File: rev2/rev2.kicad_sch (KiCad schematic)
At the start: 106 parts, among them J1 USB_C_Receptacle_USB2.0_14P, SW1 SW_SPDT, SW2 SW_SPDT, SW3 SW_SPDT, SW4 SW_SPDT, SW5 SW_SPDT, SW6 SW_SPDT, SW7 SW_SPDT, SW8 SW_SPDT, U1 ATtiny1604-SS, U2 CH340N, U3 74HC595, U4 74HC595, U5 74HC595, U6 74HC595, U7 74HC595, U8 74HC595

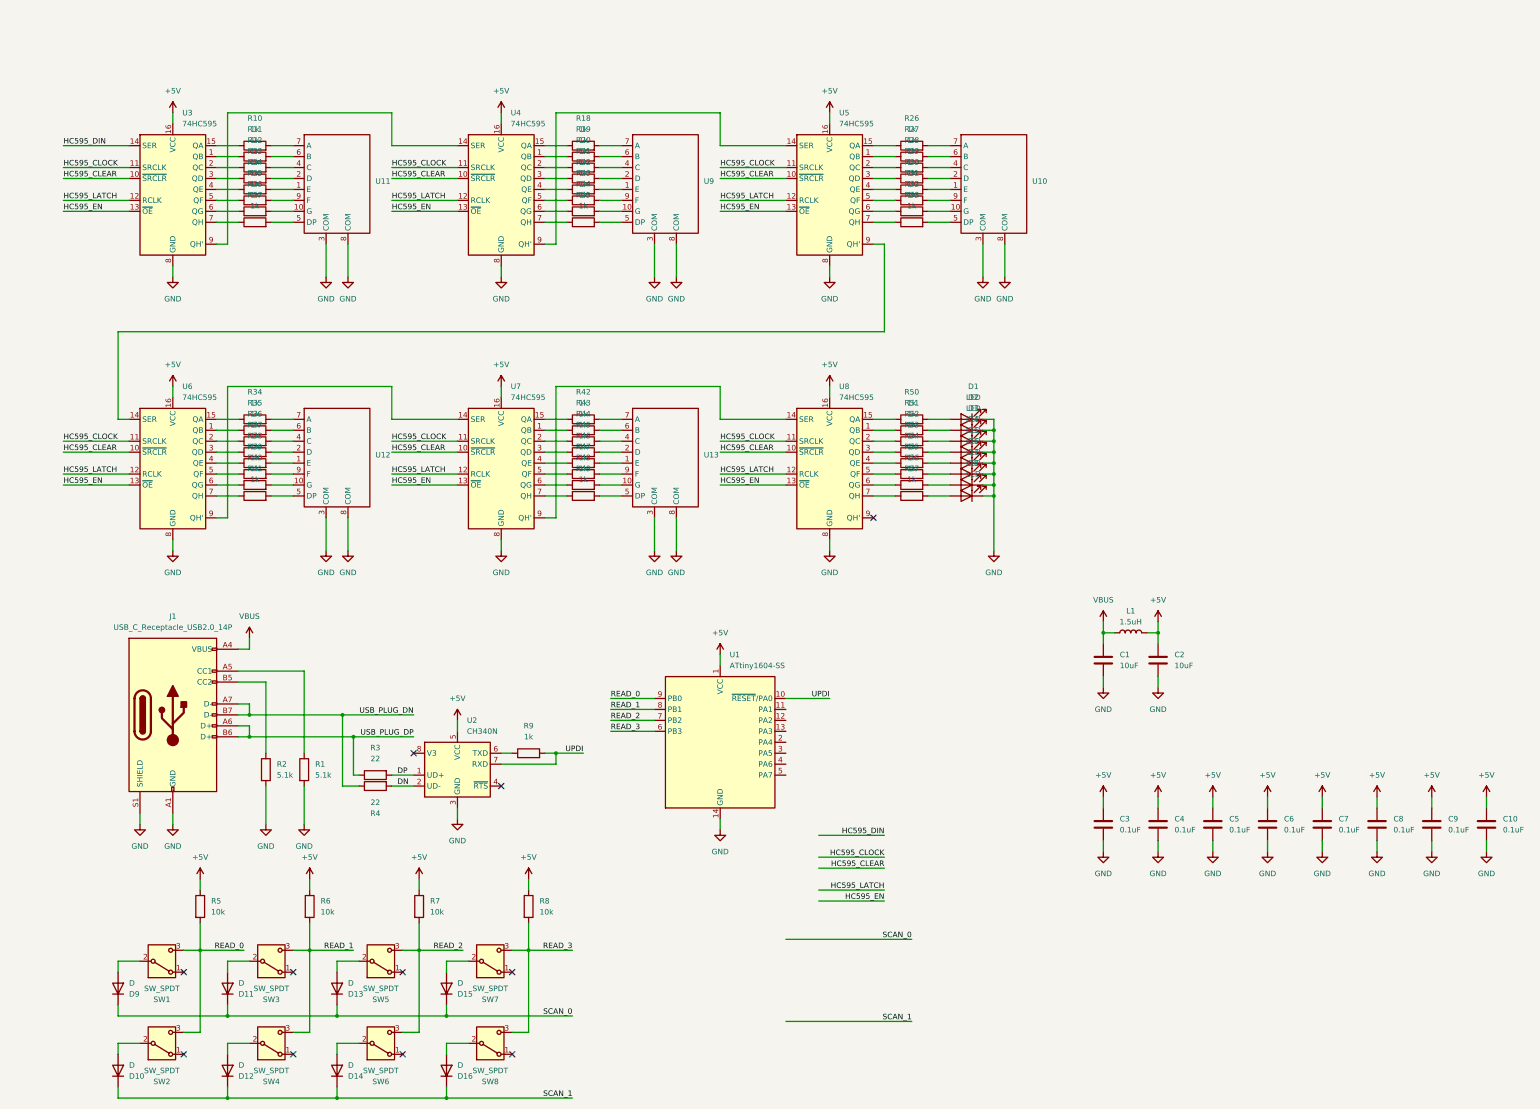
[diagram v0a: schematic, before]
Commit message: ドットマトリックスを追加してダイナミック点灯に変更
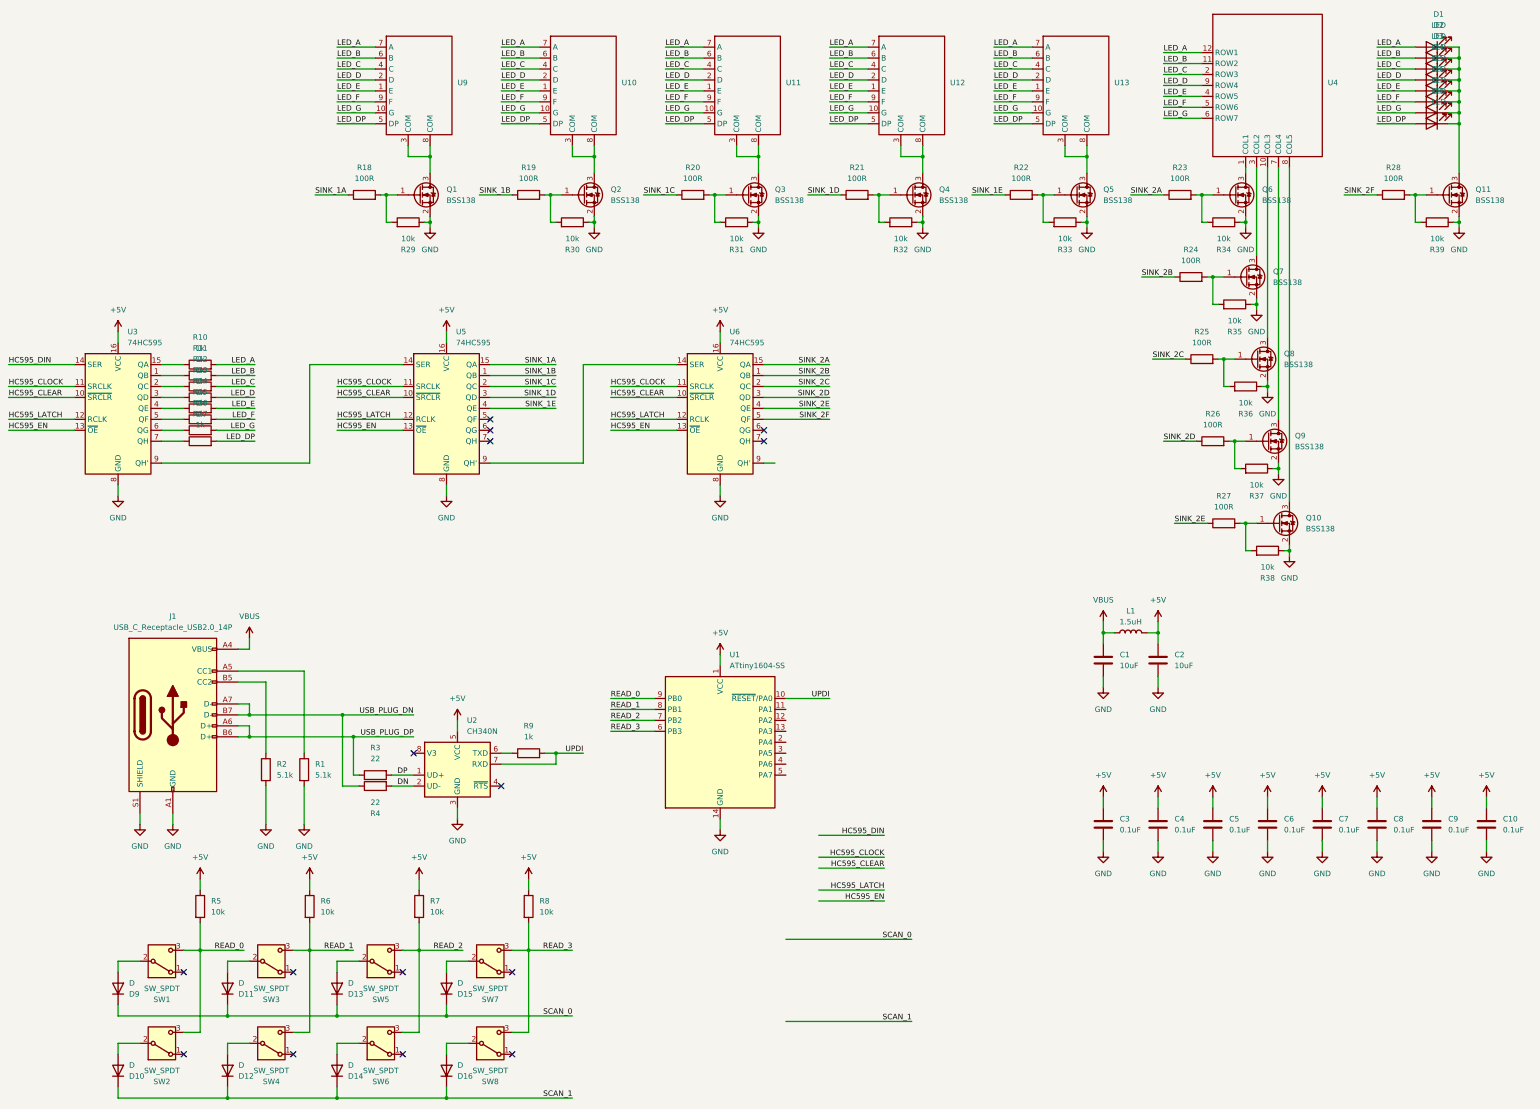
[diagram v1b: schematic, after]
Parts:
- removed R40, R41, R42, R43, R44, R45, R46, R47, R48, R49, R50, R51, R52, R53, R54, R55, R56, R57: 1k, Resistor_SMD:R_0603_1608Metric, symbol Device:R
- removed U4, U7, U8: 74HC595, Package_DFN_QFN:UQFN-16_1.8x2.6mm_P0.4mm, symbol 74xx:74HC595
- added Q1, Q10, Q11, Q2, Q3, Q4, Q5, Q6, Q7, Q8, Q9: BSS138, Package_TO_SOT_SMD:SOT-23, symbol Transistor_FET:BSS138
- added U4: ~, symbol led:5x7_dotmatrix
- R18, R19, R20, R21, R22, R23, R24, R25, R26, R27, R28: value 1k -> 100R; LCSC C22548 -> C105588
- R29, R30, R31, R32, R33, R34, R35, R36, R37, R38, R39: value 1k -> 10k; LCSC C22548 -> C98220
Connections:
- net GND: now also R29.1, R30.1, R31.1, R32.1, R33.1, R34.1, R35.1, R36.1, R37.1, R38.1, R39.1, Q1.2 (S), Q10.2 (S), Q11.2 (S), Q2.2 (S), Q3.2 (S), Q4.2 (S), Q5.2 (S), Q6.2 (S), Q7.2 (S), Q8.2 (S), Q9.2 (S); no longer D1.1 (K), D2.1 (K), D3.1 (K), D4.1 (K), D5.1 (K), D6.1 (K), D7.1 (K), D8.1 (K), U10.3 (COM), U10.8 (COM), U11.3 (COM), U11.8 (COM), U12.3 (COM), U12.8 (COM), U13.3 (COM), U13.8 (COM), U9.3 (COM), U9.8 (COM)
- net SINK_2C: now reaches U6.2 (QC)
- net SINK_2C: now also R25.1; no longer R36.1
- net at R36.2: now also R25.2, Q8.1 (G); no longer U12.4 (C)
- net LED_D: now reaches U13.2 (D)
- net LED_D: now also D4.2 (A), R13.2, U10.2 (D), U11.2 (D), U12.2 (D), U9.2 (D), U4.9 (ROW4)
- net SINK_1D: now reaches U5.3 (QD)
- net SINK_1D: now also R21.1; no longer R29.1
- net at R29.2: now also R18.2, Q1.1 (G); no longer U10.2 (D)
- net LED_DP: now reaches U9.5 (DP)
- net LED_DP: now also D8.2 (A), R17.2, U10.5 (DP), U11.5 (DP), U12.5 (DP), U13.5 (DP); no longer R25.2
- net SINK_1A: now reaches U5.15 (QA)
- net SINK_1A: now also R18.1; no longer R26.1
- net at R26.2: now also R37.2, Q9.1 (G); no longer U10.7 (A)
- net LED_E: now reaches U13.1 (E)
- net LED_E: now also D5.2 (A), R14.2, U10.1 (E), U11.1 (E), U12.1 (E), U9.1 (E), U4.4 (ROW5)
- net LED_G: now reaches U13.10 (G)
- net LED_G: now also D7.2 (A), R16.2, U10.10 (G), U11.10 (G), U12.10 (G), U9.10 (G), U4.6 (ROW7)
- net LED_C: now reaches U13.4 (C)
- net LED_C: now also D3.2 (A), R12.2, U10.4 (C), U11.4 (C), U12.4 (C), U9.4 (C), U4.2 (ROW3)
- net LED_B: now reaches U13.6 (B)
- net LED_B: now also D2.2 (A), R11.2, U10.6 (B), U11.6 (B), U12.6 (B), U9.6 (B), U4.11 (ROW2)
- net LED_A: now reaches U13.7 (A)
- net LED_A: now also D1.2 (A), R10.2, U10.7 (A), U11.7 (A), U12.7 (A), U9.7 (A), U4.12 (ROW1)
- net LED_F: now reaches U13.9 (F)
- net LED_F: now also D6.2 (A), R15.2, U10.9 (F), U11.9 (F), U12.9 (F), U9.9 (F), U4.5 (ROW6)
- net SINK_2B: now reaches U6.1 (QB)
- net SINK_2B: now also R24.1; no longer R35.1
- net at R35.2: now also R24.2, Q7.1 (G); no longer U12.6 (B)
- net at U3.9 (QH'): now also U5.14 (SER)
- net SINK_2A: now reaches U6.15 (QA)
- net SINK_2A: now also R23.1; no longer R34.1
- net SINK_2D: now reaches U6.3 (QD)
- net SINK_2D: now also R26.1; no longer R37.1
- net SINK_2E: now reaches U6.4 (QE)
- net SINK_2E: now also R27.1; no longer R38.1
- net SINK_2F: now reaches U6.5 (QF)
- net SINK_2F: now also R28.1; no longer R39.1
- net at R30.2: now also R19.2, Q2.1 (G); no longer U10.1 (E)
- net at R32.2: now also R21.2, Q4.1 (G); no longer U10.10 (G)
- net at R28.2: now also R39.2, Q11.1 (G); no longer U10.4 (C)
- net at R33.2: now also R22.2, Q5.1 (G); no longer U10.5 (DP)
- net at R27.2: now also R38.2, Q10.1 (G); no longer U10.6 (B)
- net at R31.2: now also R20.2, Q3.1 (G); no longer U10.9 (F)
- net SINK_1C: now reaches U5.2 (QC)
- net SINK_1C: now also R20.1; no longer R28.1
- net at U5.7 (QH): no longer R33.1
- net SINK_1B: now reaches R19.1
- net SINK_1B: now also U5.1 (QB)
- net SINK_1E: now reaches R22.1
- net SINK_1E: now also U5.4 (QE)
- net at U5.6 (QG): no longer R32.1
- net at U5.5 (QF): no longer R31.1
- net at R34.2: now also R23.2, Q6.1 (G); no longer U12.7 (A)
- new net: Q1.3 (D), U9.3 (COM), U9.8 (COM)
- new net: Q4.3 (D), U12.3 (COM), U12.8 (COM)
- new net: Q5.3 (D), U13.3 (COM), U13.8 (COM)
- new net: D1.1 (K), D2.1 (K), D3.1 (K), D4.1 (K), D5.1 (K), D6.1 (K), D7.1 (K), D8.1 (K), Q11.3 (D)
- new net: Q2.3 (D), U10.3 (COM), U10.8 (COM)
- new net: Q6.3 (D), U4.1 (COL1)
- new net: Q8.3 (D), U4.10 (COL3)
- new net: Q3.3 (D), U11.3 (COM), U11.8 (COM)
- new net: Q7.3 (D), U4.3 (COL2)
- new net: Q9.3 (D), U4.7 (COL4)
- new net: Q10.3 (D), U4.8 (COL5)
- no-connect marks 11 -> 15
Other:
- moved on the sheet: D1, D2, D3, D4, D5, D6, D7, D8, R10, R11, R12, R13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

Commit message: 再アノテーション
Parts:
- renumbered U13 to U10, U4 to U11, U5 to U4, U6 to U5, U9 to U6, U10 to U7, U11 to U8, U12 to U9
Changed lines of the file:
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@@
 		(dnp no)
 		(fields_autoplaced yes)
-		(property "Reference" "U13"
+		(property "Reference" "U10"
 			(at 294.64 37.4649 0)
 			(effects
@@
 			(project "rev2"
 				(path "/9a5acab1-1fb4-47d6-9caa-d2d8cb78c379"
-					(reference "U13")
+					(reference "U10")
 					(unit 1)
 				)
@@
 		(dnp no)
 		(fields_autoplaced yes)
-		(property "Reference" "U10"
+		(property "Reference" "U7"
 			(at 180.34 37.4649 0)
 			(effects
@@
 			(project "rev2"
 				(path "/9a5acab1-1fb4-47d6-9caa-d2d8cb78c379"
-					(reference "U10")
+					(reference "U7")
 					(unit 1)
 				)
@@
 		(dnp no)
 		(fields_autoplaced yes)
-		(property "Reference" "U5"
+		(property "Reference" "U4"
 			(at 141.8941 95.25 0)
 			(effects
@@
 			(project "rev2"
 				(path "/9a5acab1-1fb4-47d6-9caa-d2d8cb78c379"
-					(reference "U5")
+					(reference "U4")
 					(unit 1)
 				)
@@
 		(dnp no)
 		(fields_autoplaced yes)
-		(property "Reference" "U6"
+		(property "Reference" "U5"
 			(at 205.3941 95.25 0)
 			(effects
@@
 			(project "rev2"
 				(path "/9a5acab1-1fb4-47d6-9caa-d2d8cb78c379"
-					(reference "U6")
+					(reference "U5")
 					(unit 1)
 				)
@@
 		(dnp no)
 		(fields_autoplaced yes)
-		(property "Reference" "U12"
+		(property "Reference" "U9"
 			(at 256.54 37.4649 0)
 			(effects
@@
 			(project "rev2"
 				(path "/9a5acab1-1fb4-47d6-9caa-d2d8cb78c379"
-					(reference "U12")
+					(reference "U9")
 					(unit 1)
 				)
@@
 		(dnp no)
 		(fields_autoplaced yes)
-		(property "Reference" "U11"
+		(property "Reference" "U8"
 			(at 218.44 37.4649 0)
 			(effects
@@
 			(project "rev2"
 				(path "/9a5acab1-1fb4-47d6-9caa-d2d8cb78c379"
-					(reference "U11")
+					(reference "U8")
 					(unit 1)
 				)
@@
 		(dnp no)
 		(fields_autoplaced yes)
-		(property "Reference" "U4"
+		(property "Reference" "U11"
 			(at 344.17 37.4649 0)
 			(effects
@@
 			(project ""
 				(path "/9a5acab1-1fb4-47d6-9caa-d2d8cb78c379"
-					(reference "U4")
+					(reference "U11")
 					(unit 1)
 				)
@@
 		(dnp no)
 		(fields_autoplaced yes)
-		(property "Reference" "U9"
+		(property "Reference" "U6"
 			(at 142.24 37.4649 0)
 			(effects
@@
 			(project "rev2"
 				(path "/9a5acab1-1fb4-47d6-9caa-d2d8cb78c379"
-					(reference "U9")
+					(reference "U6")
 					(unit 1)
 				)

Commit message: 作ったフットプリントを割り当て
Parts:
- U11: footprint (none) -> led:C-2570SR
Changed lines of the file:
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@@
 			)
 		)
-		(property "Footprint" ""
+		(property "Footprint" "led:C-2570SR"
 			(at 330.2 25.4 0)
 			(effects
